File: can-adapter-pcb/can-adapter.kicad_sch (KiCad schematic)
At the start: 17 parts, among them IC1 PIC18F26Q83T-I_5N, IC2 ATA6560-GBQW-N, J1 ICSP, J2 CONN0, J3 CONN1, J4 UART, J5 CAN_PWR

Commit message: can-adapter-pcb: Add footprints for all components
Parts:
- C1: footprint (none) -> Capacitor_SMD:C_0603_1608Metric
- C2, C3, C4: footprint (none) -> Capacitor_SMD:C_0402_1005Metric
- D1: footprint (none) -> Diode_SMD:D_SOD-123
- D2: footprint (none) -> LED_SMD:LED_0402_1005Metric
- F1: footprint (none) -> Fuse:Fuse_1812_4532Metric
- IC1: footprint QFN65P600X600X100-29N-D -> PIC18F26Q83T-I/5N:QFN65P600X600X100-29N-D
- IC2: footprint SON65P300X300X90-9N-D -> ATA6560-GBQW-N:SON65P300X300X90-9N-D
- J1: footprint (none) -> Connector_PinHeader_2.54mm:PinHeader_1x06_P2.54mm_Vertical
- J2, J3: footprint (none) -> Connector_PinHeader_2.54mm:PinHeader_1x08_P2.54mm_Vertical
- J4: footprint (none) -> Connector_PinHeader_2.54mm:PinHeader_1x02_P2.54mm_Vertical
- J5: footprint (none) -> Connector_PinHeader_2.54mm:PinHeader_1x04_P2.54mm_Horizontal
- R1, R2, R3: footprint (none) -> Resistor_SMD:R_0402_1005Metric
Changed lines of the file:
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@@
 			)
 		)
-		(property "Footprint" ""
+		(property "Footprint" "Connector_PinHeader_2.54mm:PinHeader_1x06_P2.54mm_Vertical"
 			(at 163.83 58.42 0)
 			(effects
@@
 			)
 		)
-		(property "Footprint" ""
+		(property "Footprint" "Connector_PinHeader_2.54mm:PinHeader_1x02_P2.54mm_Vertical"
 			(at 241.3 59.69 0)
 			(effects
@@
 			)
 		)
-		(property "Footprint" ""
+		(property "Footprint" "Diode_SMD:D_SOD-123"
 			(at 73.66 53.34 90)
 			(effects
@@
 			)
 		)
-		(property "Footprint" ""
+		(property "Footprint" "Connector_PinHeader_2.54mm:PinHeader_1x08_P2.54mm_Vertical"
 			(at 59.69 123.19 0)
 			(effects
@@
 			)
 		)
-		(property "Footprint" ""
+		(property "Footprint" "Resistor_SMD:R_0402_1005Metric"
 			(at 115.57 49.53 0)
 			(effects
@@
 			)
 		)
-		(property "Footprint" ""
+		(property "Footprint" "Connector_PinHeader_2.54mm:PinHeader_1x04_P2.54mm_Horizontal"
 			(at 63.5 58.42 0)
 			(effects
@@
 			)
 		)
-		(property "Footprint" ""
+		(property "Footprint" "Capacitor_SMD:C_0402_1005Metric"
 			(at 34.29 135.89 0)
 			(effects
@@
 			)
 		)
-		(property "Footprint" "QFN65P600X600X100-29N-D"
+		(property "Footprint" "PIC18F26Q83T-I/5N:QFN65P600X600X100-29N-D"
 			(at 96.52 210.49 0)
 			(effects
@@
 			)
 		)
-		(property "Footprint" ""
+		(property "Footprint" "Connector_PinHeader_2.54mm:PinHeader_1x08_P2.54mm_Vertical"
 			(at 59.69 148.59 0)
 			(effects
@@
 			)
 		)
-		(property "Footprint" ""
+		(property "Footprint" "Capacitor_SMD:C_0402_1005Metric"
 			(at 151.13 134.62 0)
 			(effects
@@
 			)
 		)
-		(property "Footprint" ""
+		(property "Footprint" "Capacitor_SMD:C_0402_1005Metric"
 			(at 119.38 154.94 0)
 			(effects
@@
 			)
 		)
-		(property "Footprint" ""
+		(property "Footprint" "Capacitor_SMD:C_0603_1608Metric"
 			(at 22.86 135.89 0)
 			(effects
@@
 			)
 		)
-		(property "Footprint" ""
+		(property "Footprint" "Resistor_SMD:R_0402_1005Metric"
 			(at 119.38 147.32 0)
 			(effects
@@
 			)
 		)
-		(property "Footprint" "SON65P300X300X90-9N-D"
+		(property "Footprint" "ATA6560-GBQW-N:SON65P300X300X90-9N-D"
 			(at 200.66 221.92 0)
 			(effects
@@
 			)
 		)
-		(property "Footprint" ""
+		(property "Footprint" "Fuse:Fuse_1812_4532Metric"
 			(at 83.82 53.34 0)
 			(effects
@@
 			)
 		)
-		(property "Footprint" ""
+		(property "Footprint" "LED_SMD:LED_0402_1005Metric"
 			(at 115.57 58.42 0)
 			(effects
@@
 			)
 		)
-		(property "Footprint" ""
+		(property "Footprint" "Resistor_SMD:R_0402_1005Metric"
 			(at 110.49 151.13 0)
 			(effects

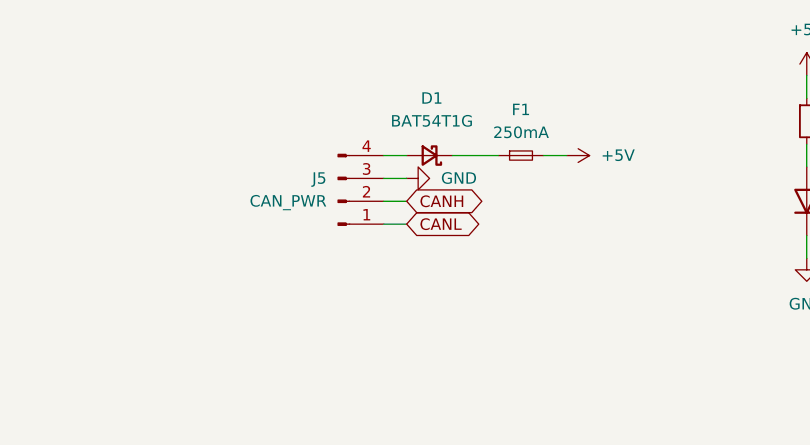
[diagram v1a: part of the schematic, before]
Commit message: can-adapter-pcb: Use polyfuse instead of regular fuse
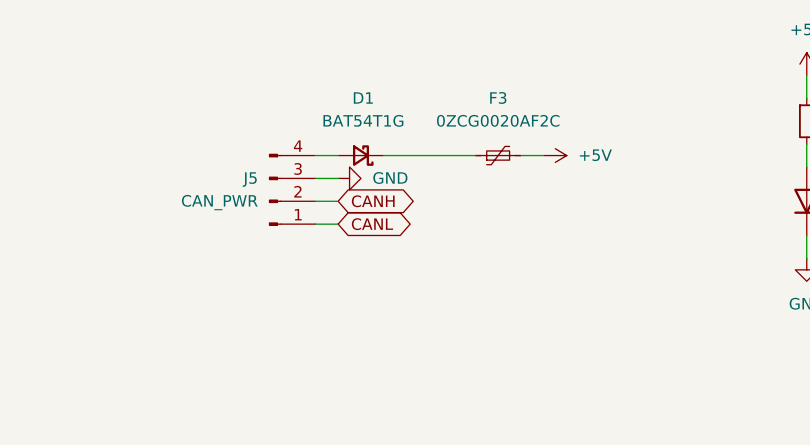
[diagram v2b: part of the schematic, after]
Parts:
- removed F1: 250mA, Fuse:Fuse_1812_4532Metric, symbol Device:Fuse_Small
- added F3: 0ZCG0020AF2C, Fuse:Fuse_1812_4532Metric, symbol Device:Polyfuse_Small
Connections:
- net +5V: now also F3.2
- net at D1.1 (K): now also F3.1
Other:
- moved on the sheet: D1, J5
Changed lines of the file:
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@@
 	(wire
 		(pts
-			(xy 88.9 53.34) (xy 86.36 53.34)
+			(xy 86.36 53.34) (xy 83.82 53.34)
 		)
 		(stroke
@@
 	(wire
 		(pts
-			(xy 68.58 53.34) (xy 71.12 53.34)
+			(xy 60.96 53.34) (xy 63.5 53.34)
 		)
 		(stroke
@@
 	(wire
 		(pts
-			(xy 68.58 55.88) (xy 71.12 55.88)
+			(xy 60.96 55.88) (xy 63.5 55.88)
 		)
 		(stroke
@@
 	(wire
 		(pts
-			(xy 68.58 60.96) (xy 71.12 60.96)
+			(xy 60.96 60.96) (xy 63.5 60.96)
 		)
 		(stroke
@@
 	(wire
 		(pts
-			(xy 68.58 58.42) (xy 71.12 58.42)
+			(xy 60.96 58.42) (xy 63.5 58.42)
 		)
 		(stroke
@@
 	(wire
 		(pts
-			(xy 76.2 53.34) (xy 81.28 53.34)
+			(xy 68.58 53.34) (xy 78.74 53.34)
 		)
 		(stroke
@@
 	(global_label "CANL"
 		(shape bidirectional)
-		(at 71.12 60.96 0)
+		(at 63.5 60.96 0)
 		(fields_autoplaced yes)
 		(effects
@@
 		)
 		(property "Intersheetrefs" "${INTERSHEET_REFS}"
-			(at 79.9337 60.96 0)
+			(at 72.3137 60.96 0)
 			(effects
 				(font
@@
 	(global_label "CANH"
 		(shape bidirectional)
-		(at 71.12 58.42 0)
+		(at 63.5 58.42 0)
 		(fields_autoplaced yes)
 		(effects
@@
 		)
 		(property "Intersheetrefs" "${INTERSHEET_REFS}"
-			(at 80.2361 58.42 0)
+			(at 72.6161 58.42 0)
 			(effects
 				(font
@@
 	(symbol
 		(lib_id "Device:D_Schottky_Small")
-		(at 73.66 53.34 180)
+		(at 66.04 53.34 180)
 		(unit 1)
 		(exclude_from_sim no)
@@
 		(fields_autoplaced yes)
 		(property "Reference" "D1"
-			(at 73.914 46.99 0)
+			(at 66.294 46.99 0)
 			(effects
 				(font
@@
 		)
 		(property "Value" "BAT54T1G"
-			(at 73.914 49.53 0)
+			(at 66.294 49.53 0)
 			(effects
 				(font
@@
 		)
 		(property "Footprint" "Diode_SMD:D_SOD-123"
-			(at 73.66 53.34 90)
+			(at 66.04 53.34 90)
 			(effects
 				(font
@@
 		)
 		(property "Datasheet" "~"
-			(at 73.66 53.34 90)
+			(at 66.04 53.34 90)
 			(effects
 				(font
@@
 		)
 		(property "Description" "Schottky diode, small symbol"
-			(at 73.66 53.34 0)
+			(at 66.04 53.34 0)
 			(effects
 				(font
@@
 	(symbol
 		(lib_id "Connector:Conn_01x04_Pin")
-		(at 63.5 58.42 0)
+		(at 55.88 58.42 0)
 		(mirror x)
 		(unit 1)
@@
 		(dnp no)
 		(property "Reference" "J5"
-			(at 62.23 55.8799 0)
+			(at 54.61 55.8799 0)
 			(effects
 				(font
@@
 		)
 		(property "Value" "CAN_PWR"
-			(at 62.23 58.4199 0)
+			(at 54.61 58.4199 0)
 			(effects
 				(font
@@
 		)
 		(property "Footprint" "Connector_PinHeader_2.54mm:PinHeader_1x04_P2.54mm_Horizontal"
-			(at 63.5 58.42 0)
+			(at 55.88 58.42 0)
 			(effects
 				(font
@@
 		)
 		(property "Datasheet" "~"
-			(at 63.5 58.42 0)
+			(at 55.88 58.42 0)
 			(effects
 				(font
@@
 		)
 		(property "Description" "Generic connector, single row, 01x04, script generated"
-			(at 63.5 58.42 0)
+			(at 55.88 58.42 0)
 			(effects
 				(font
@@
 	(symbol
 		(lib_id "power:+5V")
-		(at 88.9 53.34 270)
+		(at 86.36 53.34 270)
 		(unit 1)
 		(exclude_from_sim no)
@@
 		(fields_autoplaced yes)
 		(property "Reference" "#PWR014"
-			(at 85.09 53.34 0)
+			(at 82.55 53.34 0)
 			(effects
 				(font
@@
 		)
 		(property "Value" "+5V"
-			(at 92.71 53.3399 90)
+			(at 90.17 53.3399 90)
 			(effects
 				(font
@@
 		)
 		(property "Footprint" ""
-			(at 88.9 53.34 0)
+			(at 86.36 53.34 0)
 			(effects
 				(font
@@
 		)
 		(property "Datasheet" ""
-			(at 88.9 53.34 0)
+			(at 86.36 53.34 0)
 			(effects
 				(font
@@
 		)
 		(property "Description" "Power symbol creates a global label with name \"+5V\""
-			(at 88.9 53.34 0)
+			(at 86.36 53.34 0)
 			(effects
 				(font
@@
 	(symbol
 		(lib_id "power:GND")
-		(at 71.12 55.88 90)
+		(at 63.5 55.88 90)
 		(unit 1)
 		(exclude_from_sim no)
@@
 		(fields_autoplaced yes)
 		(property "Reference" "#PWR017"
-			(at 77.47 55.88 0)
+			(at 69.85 55.88 0)
 			(effects
 				(font
@@
 		)
 		(property "Value" "GND"
-			(at 74.93 55.8799 90)
+			(at 67.31 55.8799 90)
 			(effects
 				(font
@@
 		)
 		(property "Footprint" ""
-			(at 71.12 55.88 0)
+			(at 63.5 55.88 0)
 			(effects
 				(font
@@
 		)
 		(property "Datasheet" ""
-			(at 71.12 55.88 0)
+			(at 63.5 55.88 0)
 			(effects
 				(font
@@
 		)
 		(property "Description" "Power symbol creates a global label with name \"GND\" , ground"
-			(at 71.12 55.88 0)
+			(at 63.5 55.88 0)
 			(effects
 				(font
@@
 	)
 	(symbol
-		(lib_id "Device:Fuse_Small")
-		(at 83.82 53.34 0)
+		(lib_id "power:+5V")
+		(at 83.82 105.41 0)
 		(unit 1)
 		(exclude_from_sim no)
@@
 		(dnp no)
 		(fields_autoplaced yes)
-		(property "Reference" "F1"
-			(at 83.82 48.26 0)
+		(property "Reference" "#PWR05"
+			(at 83.82 109.22 0)
 			(effects
 				(font
 					(size 1.27 1.27)
 				)
+				(hide yes)
 			)
 		)
-		(property "Value" "250mA"
-			(at 83.82 50.8 0)
+		(property "Value" "+5V"
+			(at 83.82 100.33 0)
 			(effects
 				(font
@@
 			)
 		)
-		(property "Footprint" "Fuse:Fuse_1812_4532Metric"
-			(at 83.82 53.34 0)
+		(property "Footprint" ""
+			(at 83.82 105.41 0)
 			(effects
 				(font
@@
 			)
 		)
-		(property "Datasheet" "~"
-			(at 83.82 53.34 0)
+		(property "Datasheet" ""
+			(at 83.82 105.41 0)
 			(effects
 				(font
@@
 			)
 		)
-		(property "Description" "Fuse, small symbol"
-			(at 83.82 53.34 0)
+		(property "Description" "Power symbol creates a global label with name \"+5V\""
+			(at 83.82 105.41 0)
 			(effects
 				(font
@@
 			)
 		)
-		(pin "2"
-		)
 		(pin "1"
 		)
 		(instances
-			(project ""
+			(project "can-adapter"
 				(path "/e134d275-7c3e-44ef-bf4f-e62fff03b377"
-					(reference "F1")
+					(reference "#PWR05")
 					(unit 1)
 				)
@@
 	)
 	(symbol
-		(lib_id "power:+5V")
-		(at 83.82 105.41 0)
+		(lib_id "Device:Polyfuse_Small")
+		(at 81.28 53.34 90)
 		(unit 1)
 		(exclude_from_sim no)
@@
 		(on_board yes)
 		(dnp no)
-		(fields_autoplaced yes)
-		(property "Reference" "#PWR05"
-			(at 83.82 109.22 0)
+		(property "Reference" "F3"
+			(at 81.28 46.99 90)
 			(effects
 				(font
 					(size 1.27 1.27)
 				)
-				(hide yes)
 			)
 		)
-		(property "Value" "+5V"
-			(at 83.82 100.33 0)
+		(property "Value" "0ZCG0020AF2C"
+			(at 81.28 49.53 90)
 			(effects
 				(font
@@
 			)
 		)
-		(property "Footprint" ""
-			(at 83.82 105.41 0)
+		(property "Footprint" "Fuse:Fuse_1812_4532Metric"
+			(at 86.36 52.07 0)
 			(effects
 				(font
 					(size 1.27 1.27)
 				)
+				(justify left)
 				(hide yes)
 			)
 		)
-		(property "Datasheet" ""
-			(at 83.82 105.41 0)
+		(property "Datasheet" "~"
+			(at 81.28 53.34 0)
 			(effects
 				(font
@@
 			)
 		)
-		(property "Description" "Power symbol creates a global label with name \"+5V\""
-			(at 83.82 105.41 0)
+		(property "Description" "Resettable fuse, polymeric positive temperature coefficient, small symbol"
+			(at 81.28 53.34 0)
 			(effects
 				(font
@@
 		(pin "1"
 		)
+		(pin "2"
+		)
 		(instances
-			(project "can-adapter"
+			(project ""
 				(path "/e134d275-7c3e-44ef-bf4f-e62fff03b377"
-					(reference "#PWR05")
+					(reference "F3")
 					(unit 1)
 				)

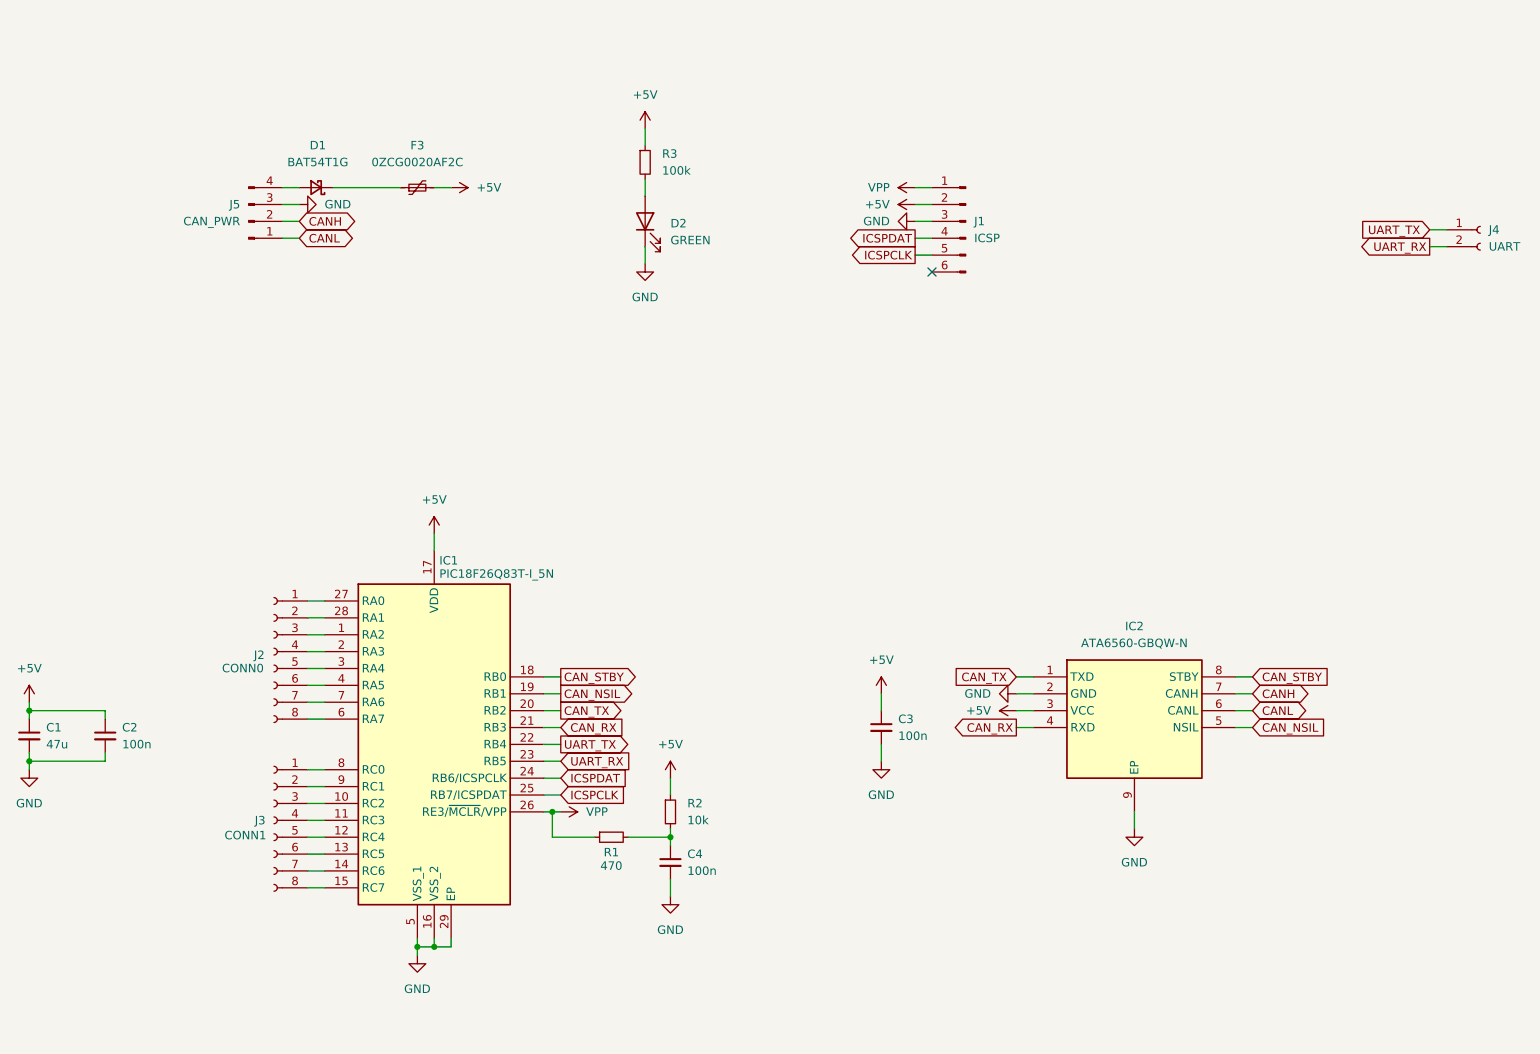
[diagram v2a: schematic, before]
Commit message: can-adapter-pcb: Create PCB
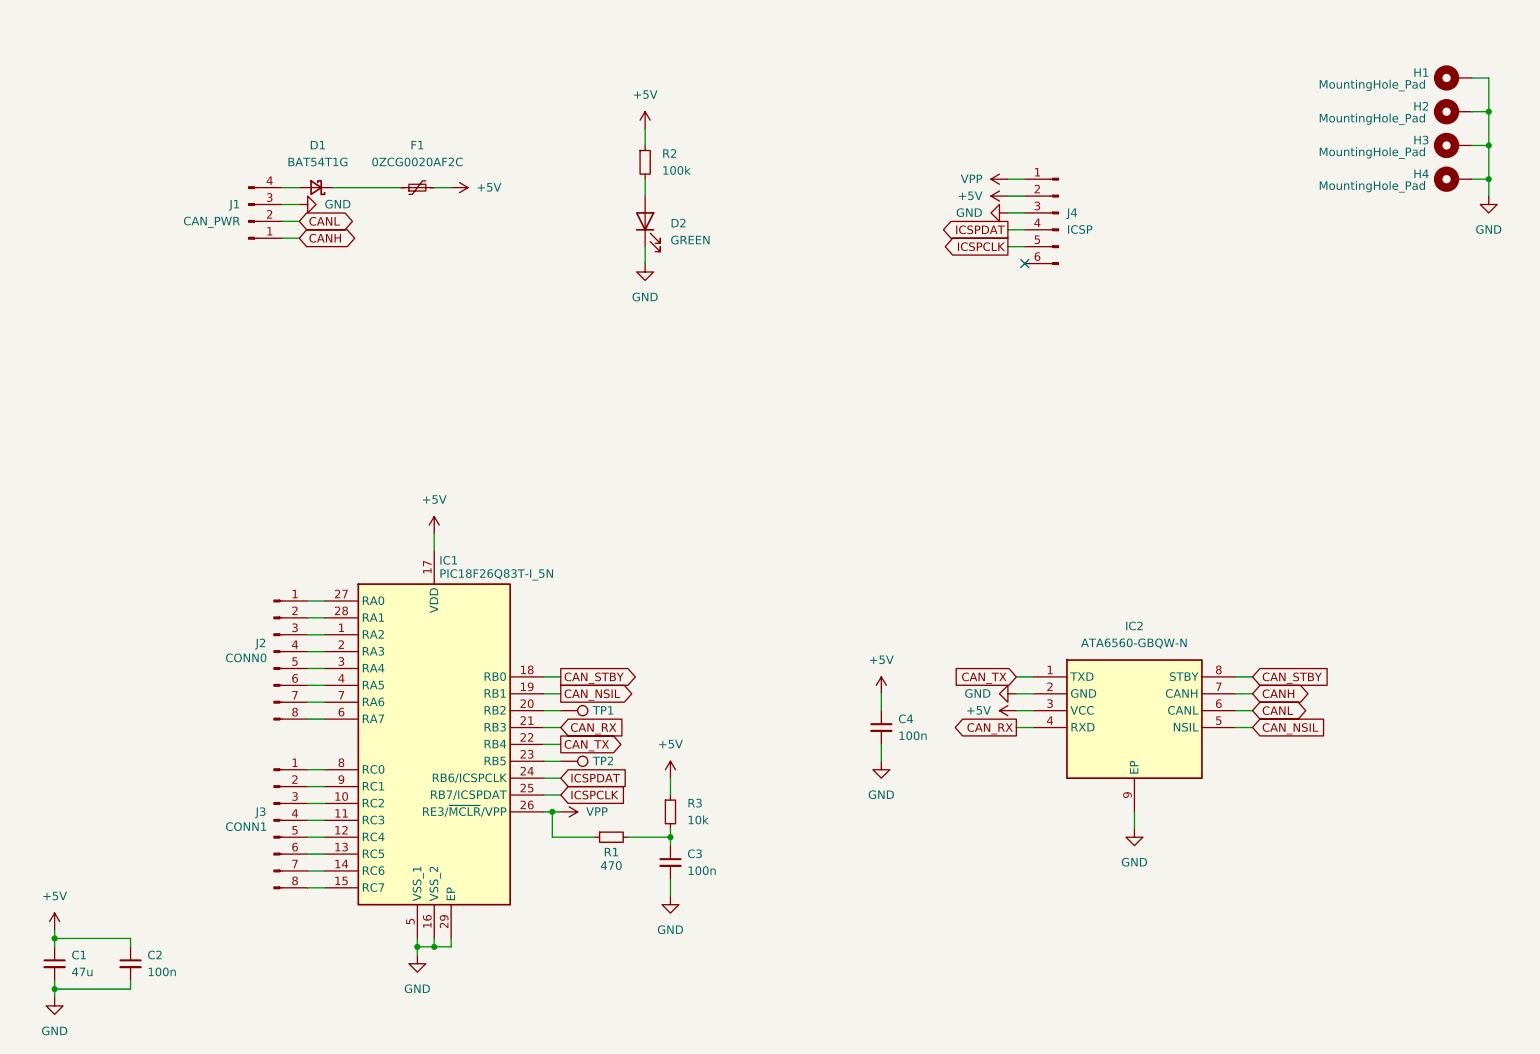
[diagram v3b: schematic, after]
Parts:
- removed J2: CONN0, Connector_PinHeader_2.54mm:PinHeader_1x08_P2.54mm_Vertical, symbol Connector:Conn_01x08_Socket
- removed J3: CONN1, Connector_PinHeader_2.54mm:PinHeader_1x08_P2.54mm_Vertical, symbol Connector:Conn_01x08_Socket
- removed J4: UART, Connector_PinHeader_2.54mm:PinHeader_1x02_P2.54mm_Vertical, symbol Connector:Conn_01x02_Socket
- added H1, H2, H3, H4: MountingHole_Pad, MountingHole:MountingHole_2.2mm_M2_Pad, symbol Mechanical:MountingHole_Pad
- added J2: CONN0, Connector_PinHeader_1.27mm:PinHeader_1x08_P1.27mm_Vertical, symbol Connector:Conn_01x08_Pin
- added J3: CONN1, Connector_PinHeader_1.27mm:PinHeader_1x08_P1.27mm_Vertical, symbol Connector:Conn_01x08_Pin
- added TP1, TP2: TestPoint, TestPoint:TestPoint_Pad_1.0x1.0mm, symbol Connector:TestPoint
- J1: renamed from J5; footprint Connector_PinHeader_2.54mm:PinHeader_1x04_P2.54mm_Horizontal -> Connector_PinHeader_2.54mm:PinHeader_1x04_P2.54mm_Vertical
- renumbered C4 to C3, C3 to C4, F3 to F1, J1 to J4, R3 to R2, R2 to R3
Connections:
- net UART_TX is gone; now on net CAN_TX: IC1.22 (RB4)
- net CANH: now also J1.1 (Pin_1); no longer J1.2 (Pin_2)
- net CANL: now also J1.2 (Pin_2); no longer J1.1 (Pin_1)
- net CAN_TX: no longer IC1.20 (RB2)
- net GND: now also H1.1, H2.1, H3.1, H4.1
- net at IC1.27 (RA0): now also J2.1 (Pin_1)
- net at IC1.28 (RA1): now also J2.2 (Pin_2)
- net at IC1.1 (RA2): now also J2.3 (Pin_3)
- net at IC1.2 (RA3): now also J2.4 (Pin_4)
- net at IC1.3 (RA4): now also J2.5 (Pin_5)
- net at IC1.4 (RA5): now also J2.6 (Pin_6)
- net at IC1.7 (RA6): now also J2.7 (Pin_7)
- net at IC1.6 (RA7): now also J2.8 (Pin_8)
- net at IC1.10 (RC2): now also J3.3 (Pin_3)
- net at IC1.11 (RC3): now also J3.4 (Pin_4)
- net at IC1.12 (RC4): now also J3.5 (Pin_5)
- net at IC1.13 (RC5): now also J3.6 (Pin_6)
- net at IC1.14 (RC6): now also J3.7 (Pin_7)
- net at IC1.15 (RC7): now also J3.8 (Pin_8)
- net at IC1.8 (RC0): now also J3.1 (Pin_1)
- net at IC1.9 (RC1): now also J3.2 (Pin_2)
- net UART_RX: no longer names the net of IC1.23 (RB5)
- net UART_RX: now also TP2.1
- new net: IC1.20 (RB2), TP1.1
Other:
- moved on the sheet: C1, C2, J4
